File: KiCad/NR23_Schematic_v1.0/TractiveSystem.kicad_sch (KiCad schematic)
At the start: 13 parts, among them M1 Zero_7R_Motor

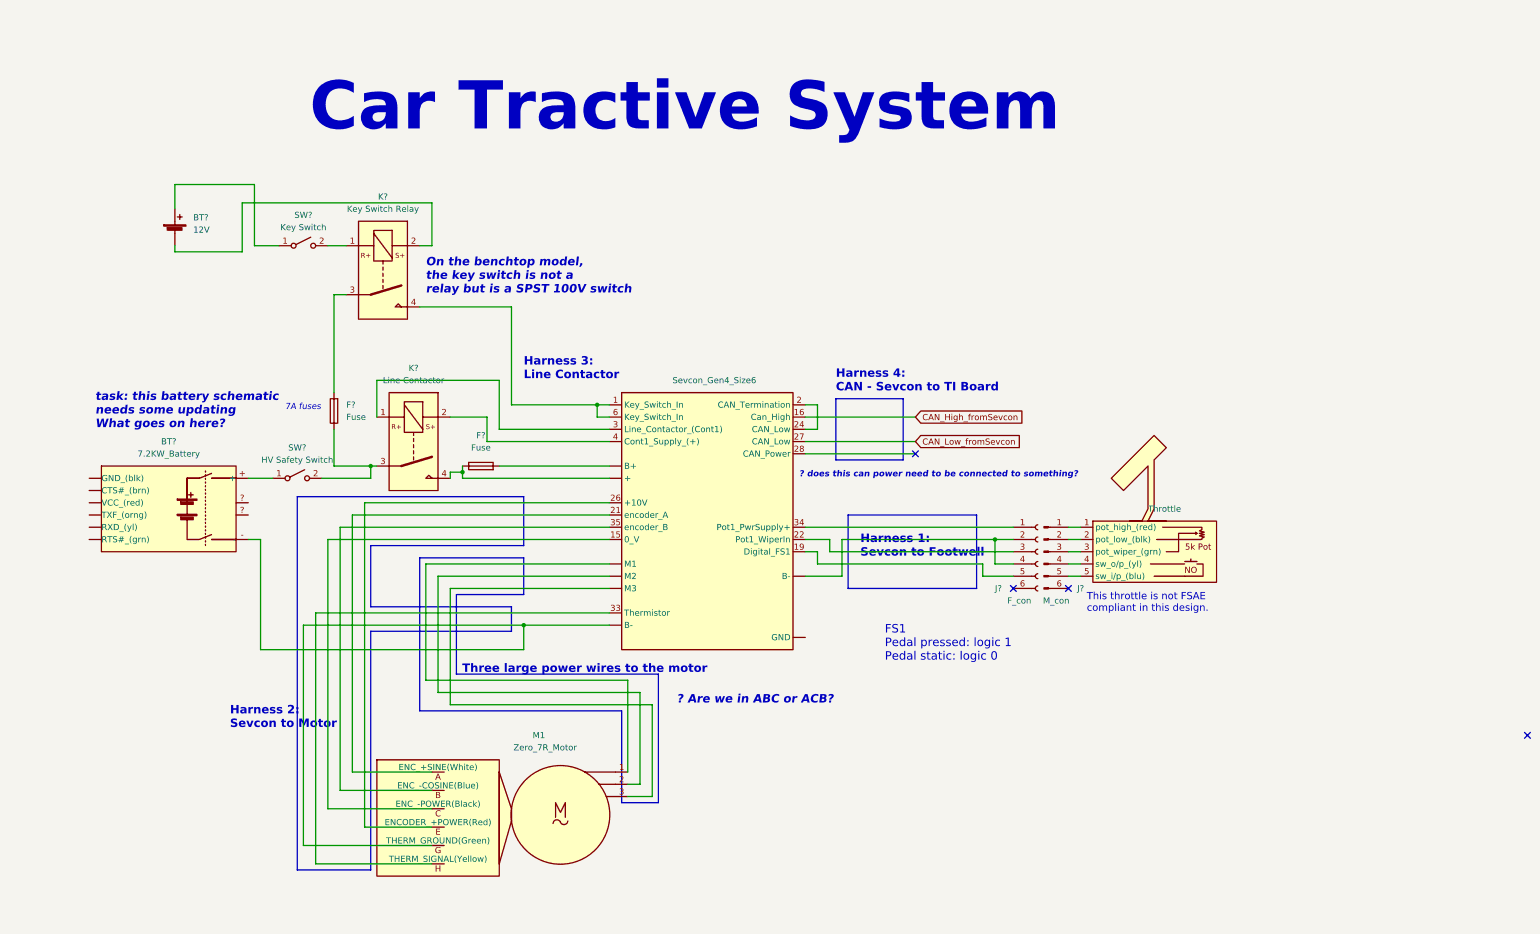
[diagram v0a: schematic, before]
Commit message: Battery update
Made big changes to the battery. Added all 16 battery pins. Started connecting the battery
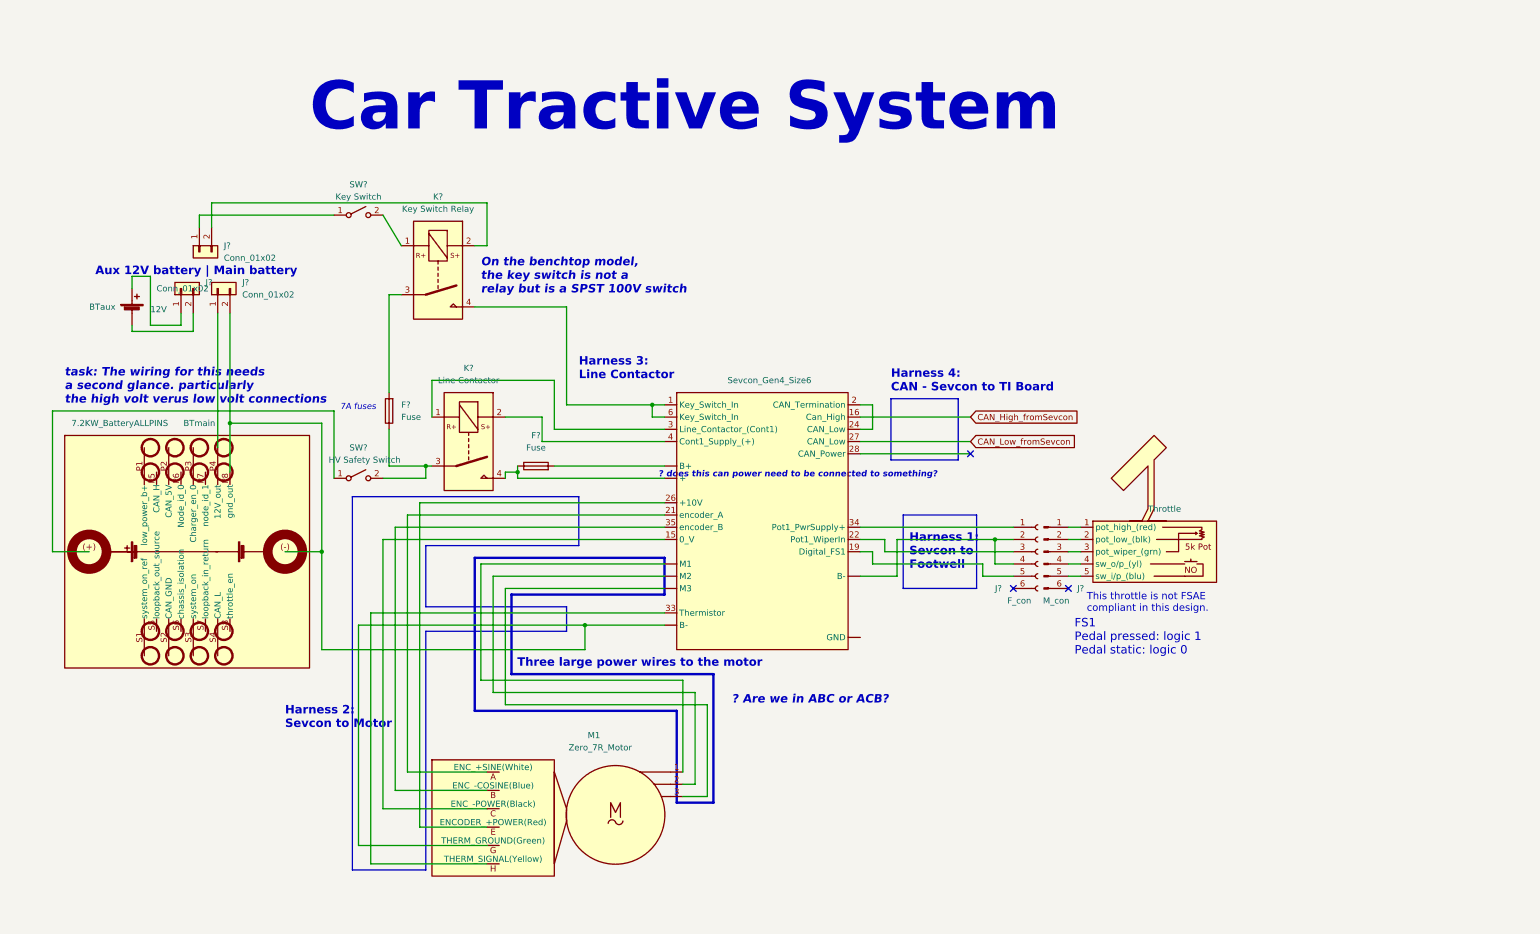
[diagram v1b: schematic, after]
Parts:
- removed BT?: 7.2KW_Battery, symbol CamachosSymbols:7.2KW_Battery
- added BTmain: 7.2KW_BatteryALLPINS, symbol CamachosSymbols:7.2KW_BatteryALLPINS
- added J? (x3): Conn_01x02, symbol Connector_Generic:Conn_01x02
- gave numbers to parts that had none: 1
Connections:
- net at M1.G (THERM_GROUND(Green)), U?. (M3): now also BTmain.(-), BTmain.P8 (gnd_out), J?.2 (Pin_2)
- net at U?. (M3): now also J?.2 (Pin_2), J?.4 (Pin_4)
- net at SW?.1 (A): now also J?.1 (Pin_1); no longer BTaux.1 (+)
- net at SW?.1 (A): now also BTmain.(+)
- net at K?.2: now also J?.2 (Pin_2); no longer BTaux.2 (-)
- new net: BTmain.P4 (12V_out), J?.1 (Pin_1)
- new net: BTaux.1 (+), J?.1 (Pin_1)
- new net: BTaux.2 (-), J?.2 (Pin_2)
- no-connect marks 4 -> 3
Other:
- note added: "Aux 12V battery | Main battery"
- note added: "task: The wiring for this needs a second glance. particularly the high volt verus low volt connections"
- note removed: "task: this battery schematic needs some updating What goes on here?"
- moved on the sheet: BTaux, F?, K?, M1, SW?

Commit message: cont. edits
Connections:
- net at U?. (M3): now also J?.2 (Pin_2), J?.4 (Pin_4)
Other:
- moved on the sheet: J?
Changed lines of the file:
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@@
     (stroke (width 0) (type default) (color 0 0 0 0))
   )
-  (polyline (pts (xy 129.54 124.46) (xy 129.54 114.3))
+  (polyline (pts (xy 146.05 124.46) (xy 146.05 114.3))
     (stroke (width 0) (type default) (color 0 0 0 0))
   )
@@
     (stroke (width 0.5) (type default) (color 0 0 0 0))
   )
-  (wire (pts (xy 50.8 58.42) (xy 50.8 55.88))
+  (wire (pts (xy 50.8 57.15) (xy 50.8 55.88))
     (stroke (width 0) (type default) (color 0 0 0 0))
   )
@@
     (stroke (width 0.5) (type default) (color 0 0 0 0))
   )
-  (polyline (pts (xy 97.79 124.46) (xy 129.54 124.46))
+  (polyline (pts (xy 97.79 124.46) (xy 146.05 124.46))
     (stroke (width 0) (type default) (color 0 0 0 0))
   )
@@
     (stroke (width 0) (type default) (color 0 0 0 0))
   )
-  (polyline (pts (xy 129.54 114.3) (xy 82.55 114.3))
+  (polyline (pts (xy 146.05 114.3) (xy 82.55 114.3))
     (stroke (width 0) (type default) (color 0 0 0 0))
   )
@@
     (stroke (width 0) (type default) (color 0 0 0 0))
   )
-  (wire (pts (xy 53.34 58.42) (xy 53.34 53.34))
+  (wire (pts (xy 53.34 57.15) (xy 53.34 53.34))
     (stroke (width 0) (type default) (color 0 0 0 0))
   )
@@
     (stroke (width 0) (type default) (color 0 0 0 0))
   )
-  (text "Harness 3:\nLine Contactor" (at 129.54 90.17 0)
+  (text "Harness 3:\nLine Contactor" (at 105.41 85.09 0)
     (effects (font (size 1.75 1.75) (thickness 0.35) bold) (justify left bottom))
   )
@@
     (effects (font (size 1.75 1.75) (thickness 0.35) bold) (justify left bottom))
   )
-  (text "Aux 12V battery | Main battery" (at 29.21 68.58 0)
+  (text "Aux 12V battery | Main battery" (at 29.21 69.85 0)
     (effects (font (size 1.75 1.75) (thickness 0.254) bold) (justify left bottom))
   )
@@
     (effects (font (size 1.75 1.75) (thickness 0.254) bold) (justify right bottom))
   )
-  (text "Car Tractive System" (at 73.66 39.37 0)
+  (text "Car Tractive System" (at 71.12 30.48 0)
     (effects (font (size 10 10) (thickness 1) bold) (justify left bottom))
   )
@@
     (effects (font (size 1.27 1.27) italic) (justify left bottom))
   )
-  (text "Harness 2:\nSevcon to Motor" (at 68.58 162.56 0)
+  (text "Harness 2:\nSevcon to\nMotor" (at 83.82 163.83 0)
     (effects (font (size 1.75 1.75) (thickness 0.35) bold) (justify left bottom))
   )
   (text "? does this can power need to be connected to something?"
-    (at 146.05 110.49 0)
+    (at 175.26 110.49 0)
     (effects (font (size 1.27 1.27) (thickness 0.254) bold italic) (justify left bottom))
   )
@@
     (pin "5")
   )
-  (symbol (lib_id "Connector_Generic:Conn_01x02") (at 50.8 63.5 90) (mirror x) (unit 1)
+  (symbol (lib_id "Connector_Generic:Conn_01x02") (at 50.8 62.23 90) (mirror x) (unit 1)
     (in_bom yes) (on_board yes) (fields_autoplaced)
-    (property "Reference" "J?" (id 0) (at 55.88 62.2299 90)
+    (property "Reference" "J?" (id 0) (at 55.88 60.9599 90)
       (effects (font (size 1.27 1.27)) (justify right))
     )
-    (property "Value" "Conn_01x02" (id 1) (at 55.88 64.7699 90)
+    (property "Value" "Conn_01x02" (id 1) (at 55.88 63.4999 90)
       (effects (font (size 1.27 1.27)) (justify right))
     )
-    (property "Footprint" "" (id 2) (at 50.8 63.5 0)
+    (property "Footprint" "" (id 2) (at 50.8 62.23 0)
       (effects (font (size 1.27 1.27)) hide)
     )
-    (property "Datasheet" "~" (id 3) (at 50.8 63.5 0)
+    (property "Datasheet" "~" (id 3) (at 50.8 62.23 0)
       (effects (font (size 1.27 1.27)) hide)
     )

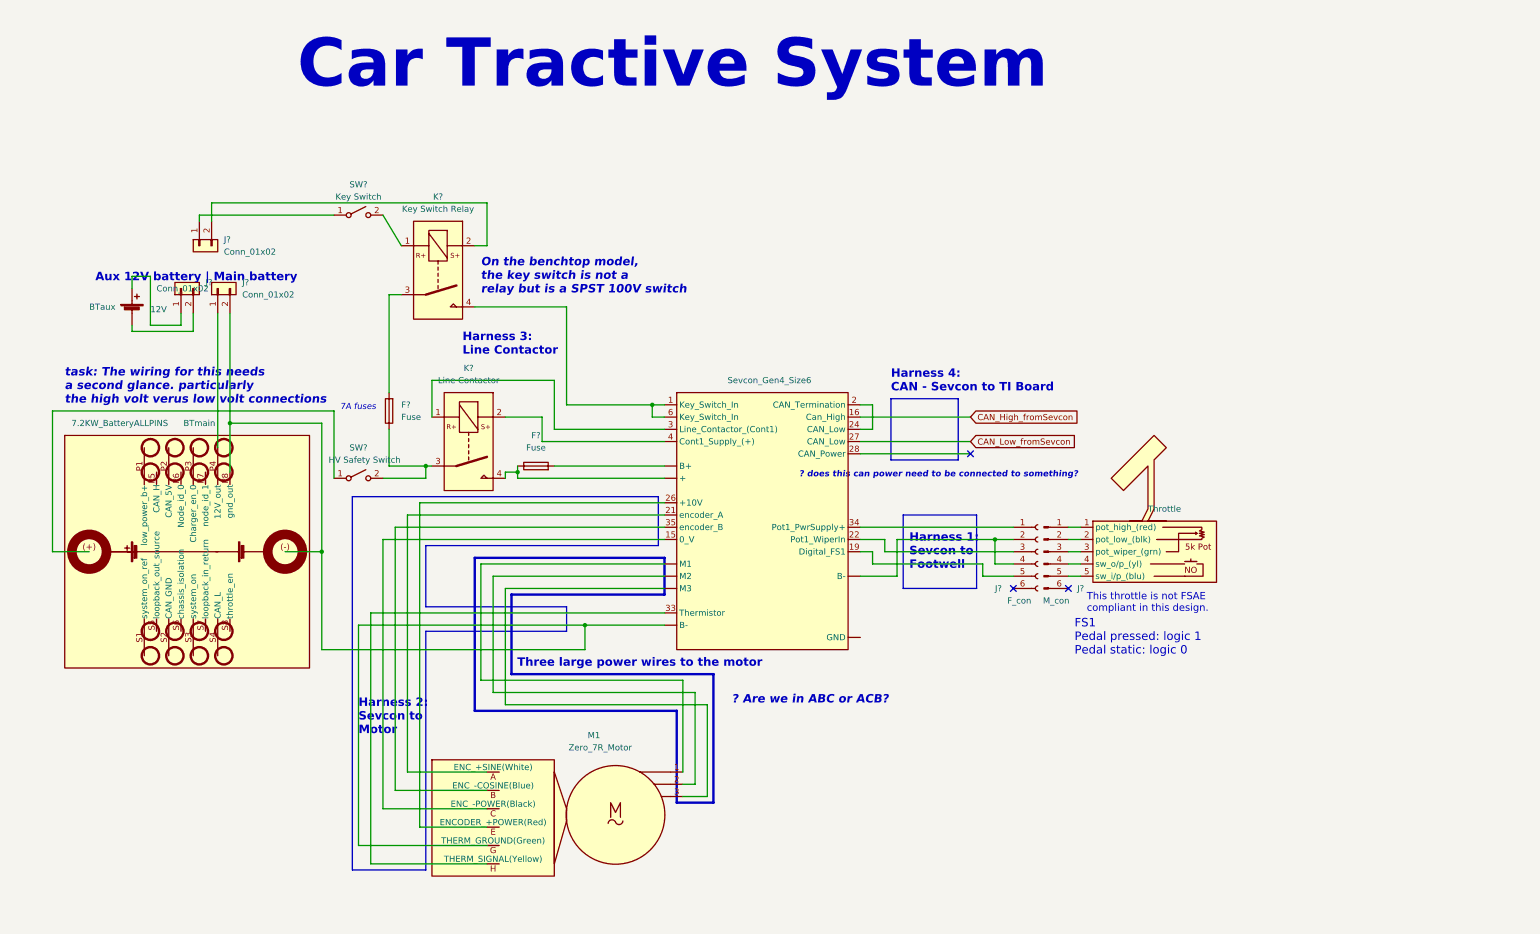
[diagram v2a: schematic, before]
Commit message: added more to the safety circuit
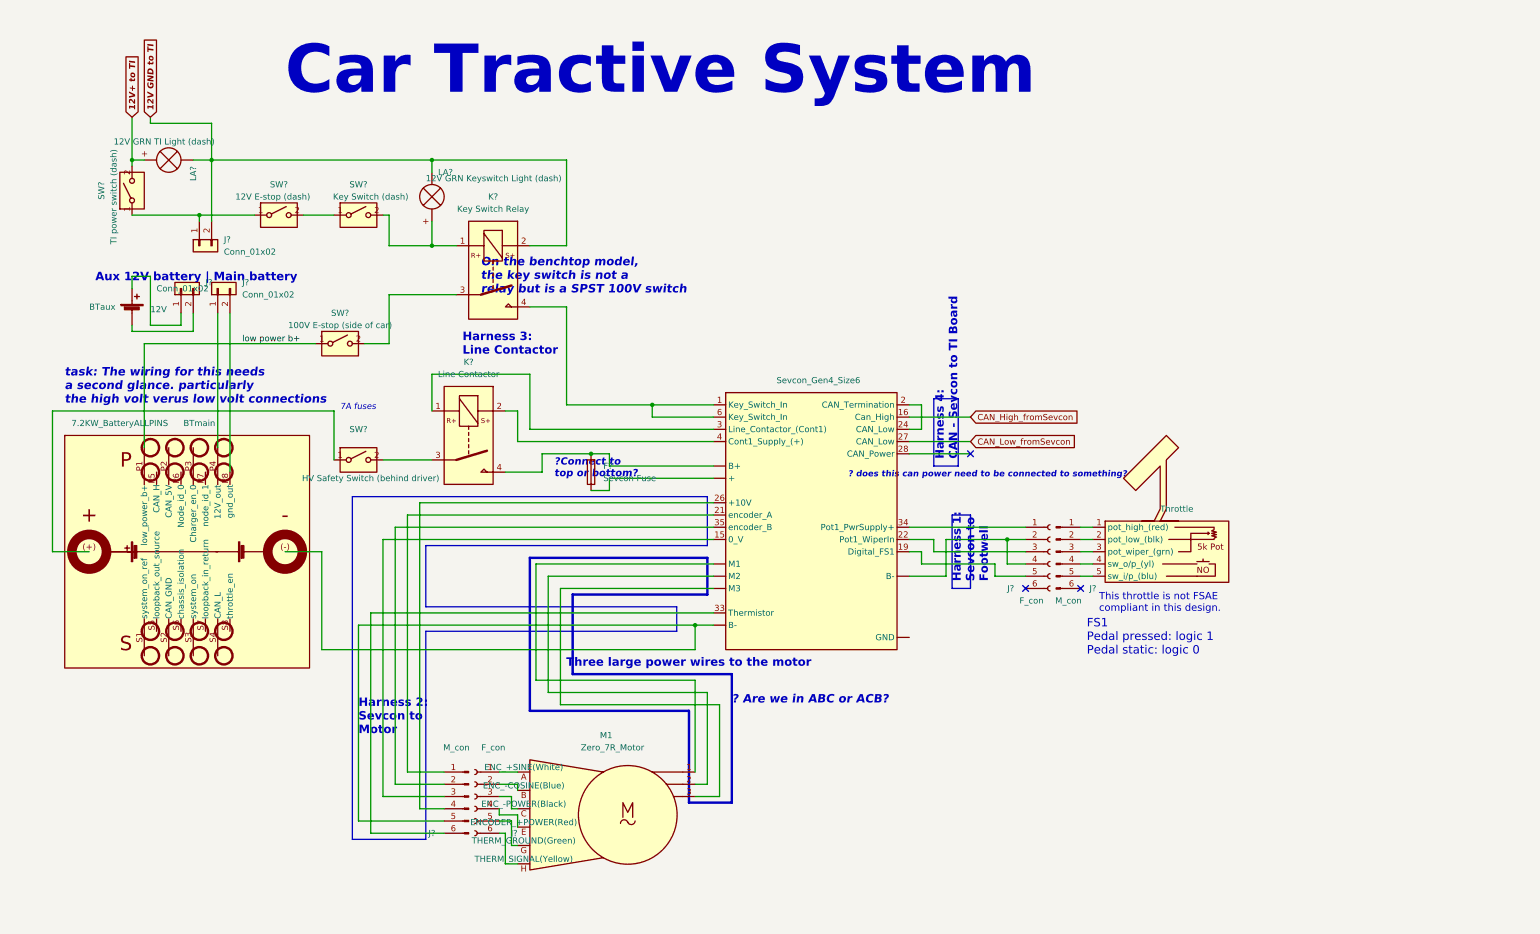
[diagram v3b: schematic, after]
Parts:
- removed F?: Fuse, symbol Device:Fuse
- added J?: M_con, symbol Connector:Conn_01x06_Male
- added J?: F_con, symbol Connector:Conn_01x06_Female
- added LA?: 12V GRN TI Light (dash), symbol Device:Lamp
- added LA?: 12V GRN Keyswitch Light (dash), symbol Device:Lamp
- added SW?: 12V E-stop (dash), symbol CamachosSymbols:SW_SPST
- added SW?: TI power switch (dash), symbol CamachosSymbols:SW_SPST
- added SW?: 100V E-stop (side of car), symbol CamachosSymbols:SW_SPST
- F?: value Fuse -> Sevcon Fuse
- SW?: value Key Switch -> Key Switch (dash); symbol Switch:SW_SPST -> CamachosSymbols:SW_SPST
- SW?: value HV Safety Switch -> HV Safety Switch (behind driver); symbol Switch:SW_SPST -> CamachosSymbols:SW_SPST
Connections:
- net at J?.1 (Pin_1): now also SW?.1 (A), SW?.1 (A); no longer SW?.1 (A)
- net 12V GND to TI: now reaches J?.2 (Pin_2), K?.2
- net 12V GND to TI: now also LA?.1 (-), LA?.1 (-)
- net at M1.A (ENC_+SINE(White)): now also J?.1 (Pin_1); no longer U?.21 (encoder_A)
- net at M1.B (ENC_-COSINE(Blue)): now also J?.2 (Pin_2); no longer U?.35 (encoder_B)
- net at M1.C (ENC_-POWER(Black)): now also J?.3 (Pin_3); no longer U?.15 (0_V)
- net at M1.E (ENCODER_+POWER(Red)): now also J?.4 (Pin_4); no longer U?.26 (+10V)
- net at M1.H (THERM_SIGNAL(Yellow)): now also J?.6 (Pin_6); no longer U?.33 (Thermistor)
- net at U?. (M3): now also J?.2 (Pin_2), J?.4 (Pin_4)
- net at F?.2, U?. (M3): now also K?.4
- net at K?.1, SW?.2 (B): now also LA?.2 (+)
- net at K?.3: now also SW?.2 (B)
- net low power b+: now reaches BTmain.P1 (low_power_b+)
- net low power b+: now also SW?.1 (A)
- new net: J?.5 (Pin_5), M1.G (THERM_GROUND(Green))
- new net: BTmain.(-), J?.5 (Pin_5), U?. (M3)
- new net: F?.1, U?. (M3)
- new net: J?.3 (Pin_3), U?.15 (0_V)
- new net: J?.1 (Pin_1), U?.21 (encoder_A)
- new net: J?.4 (Pin_4), U?.26 (+10V)
- new net: J?.6 (Pin_6), U?.33 (Thermistor)
- new net: J?.2 (Pin_2), U?.35 (encoder_B)
- new net: SW?.1 (A), SW?.2 (B)
- new net: BTmain.P8 (gnd_out), J?.2 (Pin_2)
- new net 12V+ to TI: LA?.2 (+), SW?.2 (B)
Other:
- note added: "?Connect to top or bottom?"
- moved on the sheet: F?, J?, K?
